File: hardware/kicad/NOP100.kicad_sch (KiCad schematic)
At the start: 44 parts, among them CON1 MIKROBUS_MODULE_CONN, CON2 MIKROBUS_MODULE_CONN, J1 CAN, Q1 BSS138, Q2 BSS138, SW1 BUS, SW2 SW_Push, U1 NCS1S1205SC, U2 MCP2551-I-P, U3 Teensy_4.0, U4 74HC165, U6 NCS1S1203SC

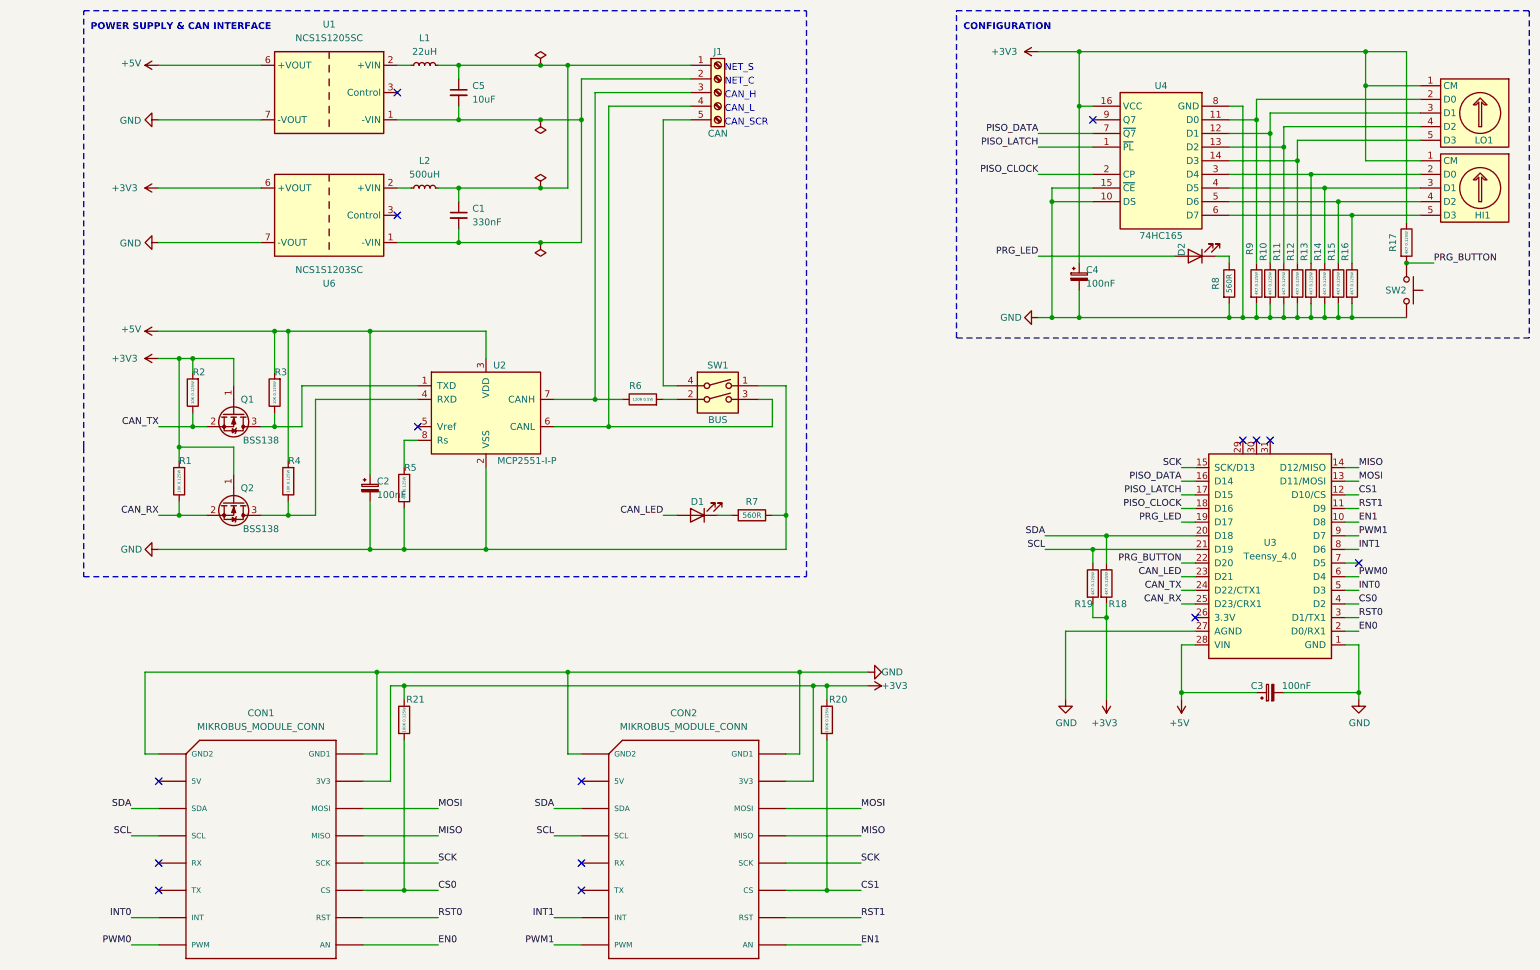
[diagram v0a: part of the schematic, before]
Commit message: Revise mikrobus symbol
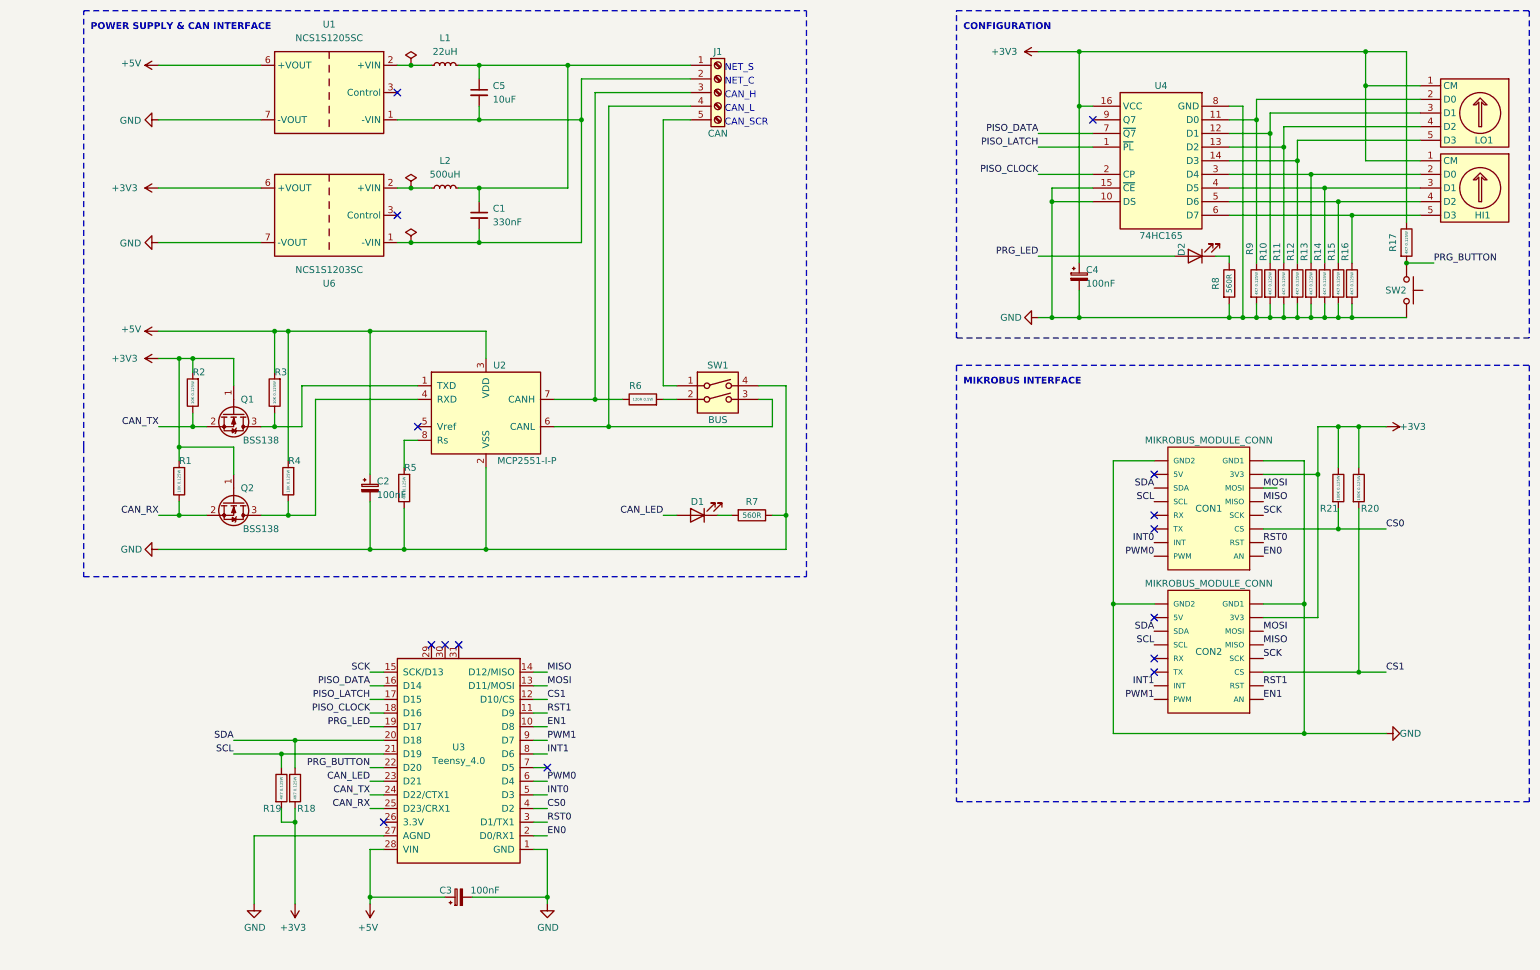
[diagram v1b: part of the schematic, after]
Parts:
- CON1, CON2: symbol mikroBUS:MIKROBUS_MODULE_CONN -> pdjr:MIKROBUS_MODULE_CONN
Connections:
- net GND: now also SW1.4; no longer SW1.1
- net at J1.5 (Pin_5): now also SW1.1; no longer SW1.4
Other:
- note added: "MIKROBUS INTERFACE"
- moved on the sheet: C1, C3, C5, L1, L2, R18, R19, R20, R21, U3

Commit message: Update README
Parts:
- C2, C3, C4: symbol Device:C_Polarized_Small -> Device:C_Small
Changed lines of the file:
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@@
     )
   )
-  (symbol (lib_id "Device:C_Polarized_Small") (at 67.31 102.87 0) (unit 1)
+  (symbol (lib_id "Device:C_Small") (at 67.31 102.87 0) (unit 1)
     (in_bom yes) (on_board yes) (dnp no)
     (property "Reference" "C2" (at 68.58 101.6 0)
@@
     )
   )
-  (symbol (lib_id "Device:C_Polarized_Small") (at 199.39 63.5 0) (unit 1)
+  (symbol (lib_id "Device:C_Small") (at 199.39 63.5 0) (unit 1)
     (in_bom yes) (on_board yes) (dnp no)
     (property "Reference" "C4" (at 200.66 62.23 0)
@@
     )
   )
-  (symbol (lib_id "Device:C_Polarized_Small") (at 83.82 179.07 90) (unit 1)
+  (symbol (lib_id "Device:C_Small") (at 83.82 179.07 90) (unit 1)
     (in_bom yes) (on_board yes) (dnp no)
     (property "Reference" "C3" (at 82.55 177.8 90)
